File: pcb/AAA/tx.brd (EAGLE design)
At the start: 28 x 35 mm, 52 parts, among them U3 MCP73831T-2ACI/OT, Y1 CRYSTAL-26MHZSMD-3.2X2.5

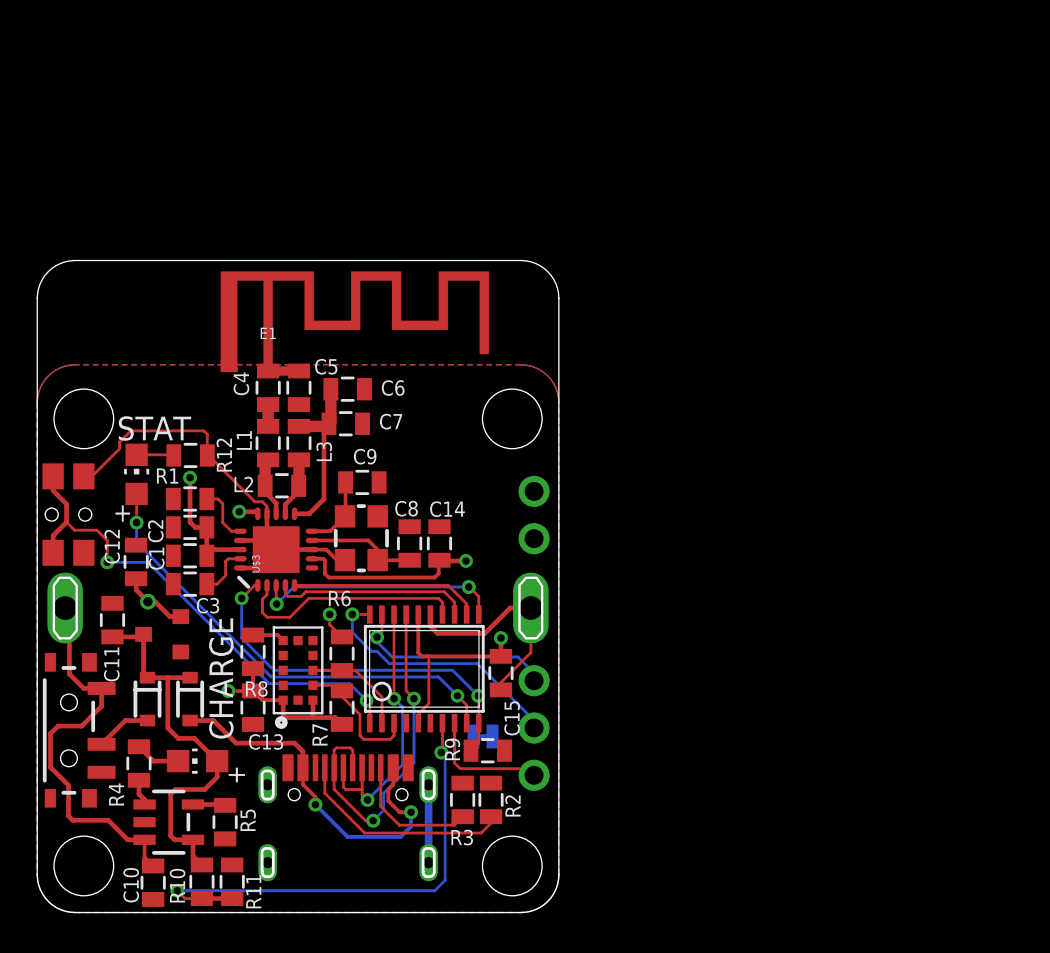
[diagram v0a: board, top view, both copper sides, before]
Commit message: usb on tx
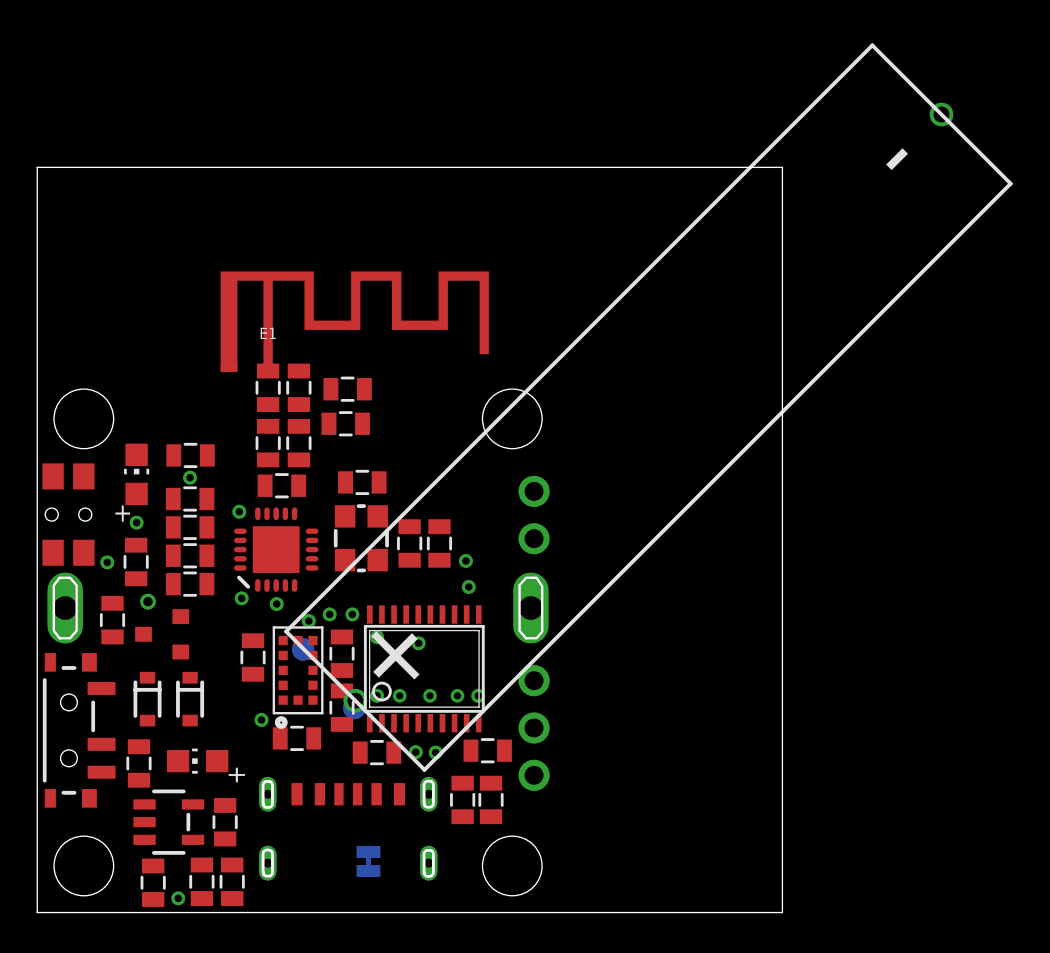
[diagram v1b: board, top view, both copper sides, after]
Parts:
- added TP1, TP2: TPTP12R, testpad:TP12R
- added U$1: L1_USBC_6P_DEV, tx:L1_USBC_6P_PAC
- U$4: value USBC_16P -> AAA_SYM; device my_usbc_16p:USBC_16P_FOOT -> 3pos_slide_switch:AAAWTF
- moved U$4 26.7 mm to (32.5, 26.5), turned to 45 degrees
- moved SJ2 9.10 mm to (17.8, 2.74), turned to 90 degrees
- moved C15 7.91 mm to (18.2, 8.59), turned to 180 degrees
- moved C13 2.88 mm to (13.9, 9.35), turned to 0 degrees
- moved R8 0.30 mm to (11.6, 13.7)
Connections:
- removed net N$23: R6.1, U$2.2, U1.9
- new net N$36: TP1.TP, U1.7
- new net N$37: TP2.TP, U$2.2
- net GND: now also U$1.1, U$1.2, U$1.3, U$1.4, U$1.GND1, U$1.GND2, U$2.1; no longer U$4.A1B12, U$4.B11A12, U$4.P$13, U$4.P$14, U$4.P$15, U$4.P$16
- net N$10: now also U$1.CC2; no longer U$4.B5
- net N$11: now also U$1.CC1; no longer U$4.A5
- net N$18: now also R6.1, U1.9; no longer U$4.A6, U$4.B6
- net N$22: now also U$2.17; no longer U$2.3
- net N$26: now also U$1.VBUS1, U$1.VBUS2; no longer U$4.A4B9, U$4.B4A9
- net N$30: now also U$2.6; no longer U$2.1
- net N$34: now also SJ2.2, U$2.3; no longer U$2.17, U$4.A7, U$4.B7
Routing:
- net +3V3: track 43.8 -> 0.00 mm, vias 7 -> 8
- net GND: track 39.6 -> 0.00 mm
- net N$30: track 26.7 -> 0.00 mm
- net N$35: track 26.3 -> 0.00 mm
- net N$29: track 24.9 -> 0.00 mm
- net N$27: track 21.3 -> 0.00 mm
- net N$25: track 21.0 -> 0.00 mm
- net N$21: track 20.4 -> 0.00 mm
- net N$26: track 20.1 -> 0.00 mm, vias 2 -> 0
- net N$34: track 19.1 -> 0.00 mm, vias 2 -> 1
- net N$18: track 14.9 -> 0.00 mm, vias 2 -> 0
- net N$32: track 14.0 -> 0.00 mm
- net N$16: track 13.4 -> 0.00 mm
- net N$20: track 12.5 -> 0.00 mm
- net N$11: track 11.7 -> 0.00 mm
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- removed copper zone on layer 16, net +3V3
- removed copper zone on layer 1, net GND
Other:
- board size 28 x 35 mm -> 40 x 40 mm
- board text removed: "-"
- board text removed: "3V"
- board text removed: "CHARGE"
- board text removed: "CLK"
- board text removed: "DIO"
- board text removed: "GND"
- board text removed: "OFF"
- board text removed: "ON"
- board text removed: "STAT"
- board text removed: "TEST"
- board text removed: "TX"
- board text removed: "dayTripper TX dekuNukem 2018"
- board text removed: "git.io/daytripper"
